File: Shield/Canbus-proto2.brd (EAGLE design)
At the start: 92.7 x 53.3 mm, 82 parts, among them J1 Digital_0_7, J2 Analog, J3 Digital_8_13, J4 Analog, J5 Digital_14_21

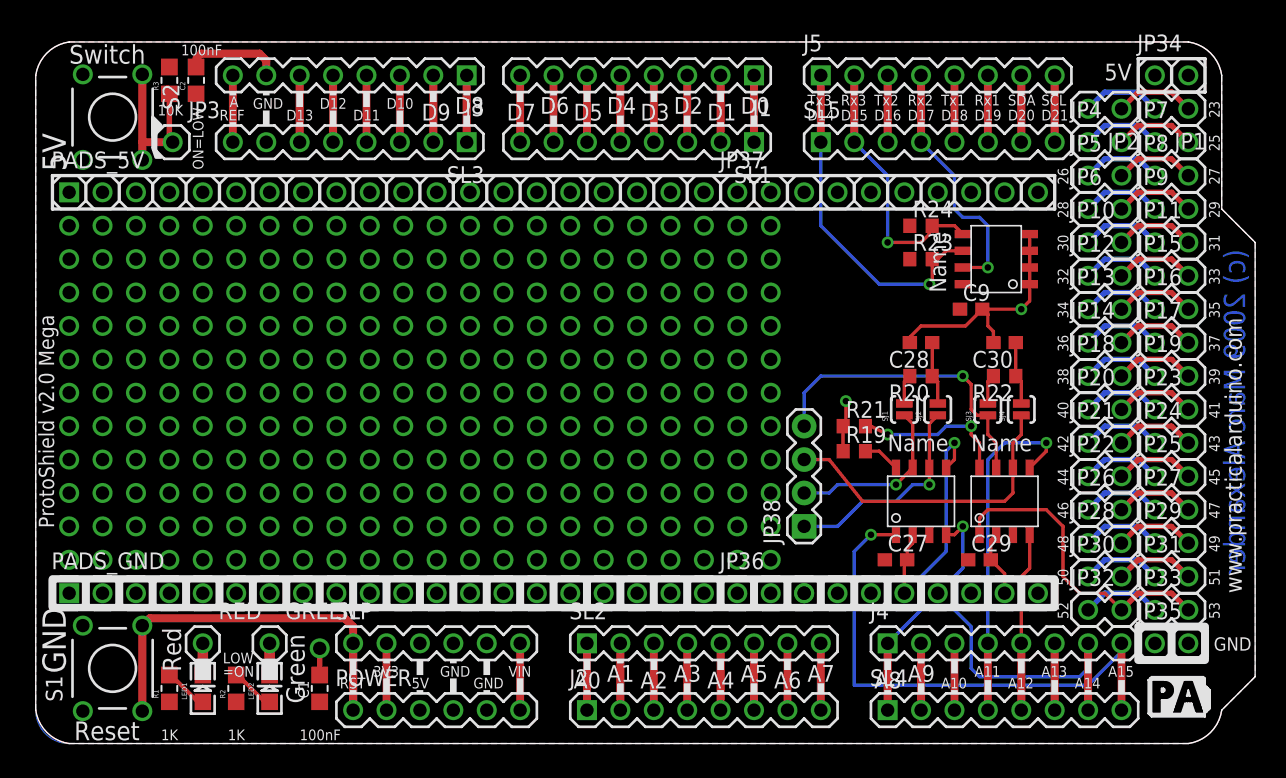
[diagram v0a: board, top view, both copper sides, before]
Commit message: Updated board design for canbus shield. There are now RJ45 ports for canbus outputs and a little SMD proto space.
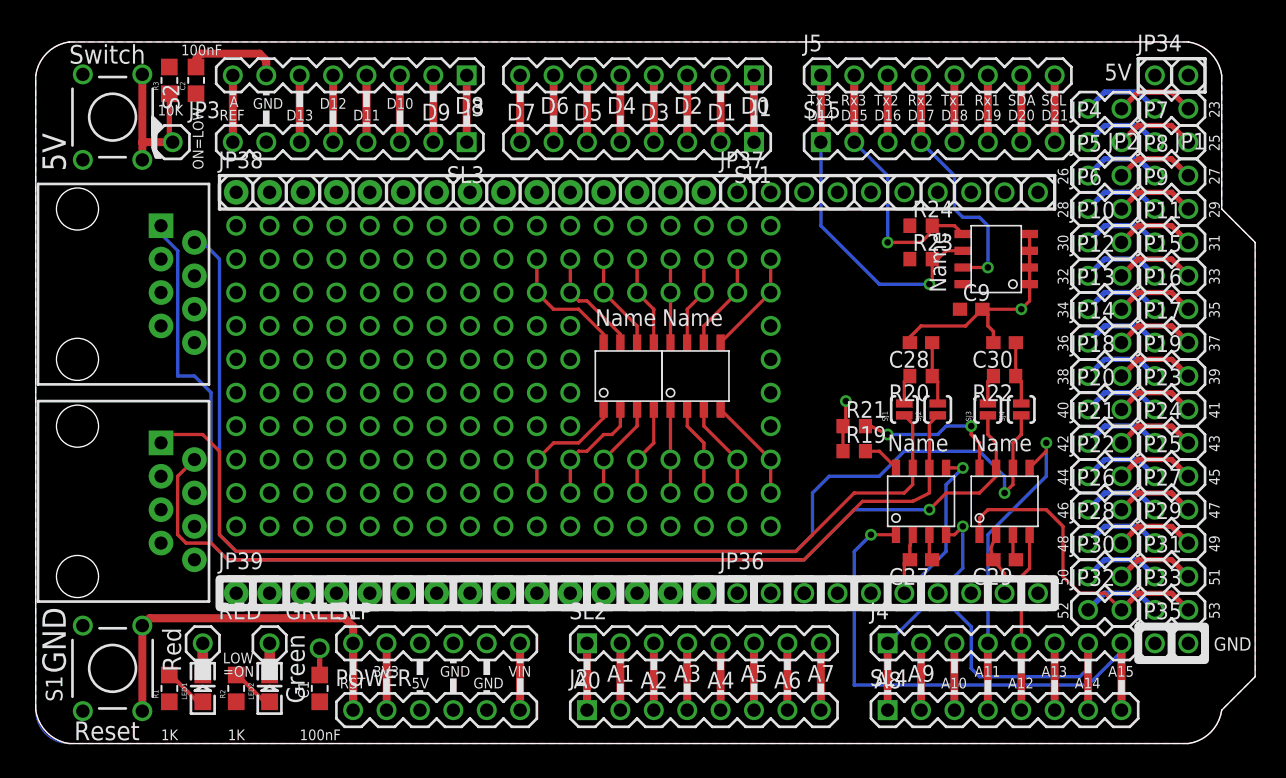
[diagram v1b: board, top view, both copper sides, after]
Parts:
- removed PADS_5V, PADS_GND: M20, SparkFun:1X20
- added JP39: M15, SparkFun-Connectors:1X15
- added U$1, U$2: RJ45-8PTH, SparkFun-Connectors:RJ45-8
- added U$3: SN65HVD234, ck_custom:SOIC8
- JP38: value (none) -> M15; device SparkFun-Connectors:1X04 -> SparkFun-Connectors:1X15
- U$4: value (none) -> SN65HVD234; device SparkFun:PRACTICALARDUINO-LOGO -> ck_custom:SOIC8
- moved JP38 50.1 mm to (15.2, 41.9), turned to 0 degrees
- moved U$4 48.4 mm to (42.5, 26.0)
- moved C27 1.91 mm to (67.3, 14.0), turned to 180 degrees
- moved C29 1.91 mm to (73.7, 14.0), turned to 180 degrees
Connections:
- new net B1: U$3.PIN8
- new net B10: U$4.PIN7
- new net B11: U$4.PIN6
- new net B12: U$4.PIN5
- new net B13: U$4.PIN4
- new net B14: U$4.PIN3
- new net B15: U$4.PIN2
- new net B16: U$4.PIN1
- new net B2: U$3.PIN7
- new net B3: U$3.PIN6
- new net B4: U$3.PIN5
- new net B5: U$3.PIN1
- new net B6: U$3.PIN2
- new net B7: U$3.PIN3
- new net B8: U$3.PIN4
- new net B9: U$4.PIN8
- net +3V3: now also JP38.1, JP38.10, JP38.11, JP38.12, JP38.13, JP38.14, JP38.15, JP38.2, JP38.3, JP38.4, JP38.5, JP38.6, JP38.7, JP38.8, JP38.9; no longer PADS_5V.1, PADS_5V.10, PADS_5V.11, PADS_5V.12, PADS_5V.13, PADS_5V.14, PADS_5V.15, PADS_5V.16, PADS_5V.17, PADS_5V.18, PADS_5V.19, PADS_5V.2, PADS_5V.20, PADS_5V.3, PADS_5V.4, PADS_5V.5, PADS_5V.6, PADS_5V.7, PADS_5V.8, PADS_5V.9
- net CANH0: now also U$2.1; no longer JP38.2
- net CANH1: now also U$1.1; no longer JP38.4
- net CANL0: now also U$2.2; no longer JP38.1
- net CANL1: now also U$1.2; no longer JP38.3
- net GND: now also JP39.1, JP39.10, JP39.11, JP39.12, JP39.13, JP39.14, JP39.15, JP39.2, JP39.3, JP39.4, JP39.5, JP39.6, JP39.7, JP39.8, JP39.9, U$1.3, U$1.7, U$2.3, U$2.7; no longer PADS_GND.1, PADS_GND.10, PADS_GND.11, PADS_GND.12, PADS_GND.13, PADS_GND.14, PADS_GND.15, PADS_GND.16, PADS_GND.17, PADS_GND.18, PADS_GND.19, PADS_GND.2, PADS_GND.20, PADS_GND.3, PADS_GND.4, PADS_GND.5, PADS_GND.6, PADS_GND.7, PADS_GND.8, PADS_GND.9
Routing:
- net CANL1: track 23.8 -> 97.1 mm, vias 0 -> 1
- net CANH1: track 23.6 -> 94.2 mm
- net CANH0: track 13.3 -> 72.4 mm, vias 1 -> 0
- net CANL0: track 16.4 -> 72.3 mm, vias 1 -> 0
- net B9: track 0.00 -> 9.57 mm, vias 0 -> 2
- net B16: track 0.00 -> 9.57 mm, vias 0 -> 2
- net B15: track 0.00 -> 8.67 mm, vias 0 -> 2
- net B10: track 0.00 -> 8.30 mm, vias 0 -> 2
- net B8: track 0.00 -> 7.93 mm, vias 0 -> 2
- net B4: track 0.00 -> 7.93 mm, vias 0 -> 2
- net B7: track 0.00 -> 7.40 mm, vias 0 -> 2
- net B3: track 0.00 -> 7.40 mm, vias 0 -> 2
- net B14: track 0.00 -> 7.40 mm, vias 0 -> 2
- net B11: track 0.00 -> 7.40 mm, vias 0 -> 2
- net B12: track 0.00 -> 6.88 mm, vias 0 -> 2
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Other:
- board text removed: "(c) 2009 Marc Alexander"
- board text removed: "ProtoShield v2.0 Mega"
- board text removed: "www.practicalarduino.com"

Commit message: Updated the board to be more better and junk.
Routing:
- net GND: track 41.6 -> 48.0 mm, vias 4 -> 6
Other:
- board size 92.7 x 53.3 mm -> 92.8 x 53 mm
- board text added: "CAN1"
- board text added: "CAN2"
- board text added: "Due CAN Shield V 1.0"
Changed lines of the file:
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@@
 <layer number="20" name="Dimension" color="15" fill="1" visible="yes" active="yes"/>
 <layer number="21" name="tPlace" color="16" fill="1" visible="yes" active="yes"/>
-<layer number="22" name="bPlace" color="14" fill="1" visible="no" active="yes"/>
+<layer number="22" name="bPlace" color="14" fill="1" visible="yes" active="yes"/>
 <layer number="23" name="tOrigins" color="15" fill="1" visible="yes" active="yes"/>
 <layer number="24" name="bOrigins" color="15" fill="1" visible="no" active="yes"/>
@@
 <board>
 <plain>
-<wire x1="0" y1="2.54" x2="2.54" y2="0" width="0" layer="20" curve="73.740878"/>
-<wire x1="87.63" y1="0" x2="90.17" y2="2.54" width="0" layer="20" curve="73.740878"/>
-<wire x1="90.17" y1="2.54" x2="92.71" y2="5.08" width="0" layer="20"/>
-<wire x1="92.71" y1="5.08" x2="92.71" y2="38.1" width="0" layer="20"/>
-<wire x1="92.71" y1="38.1" x2="90.17" y2="40.64" width="0" layer="20"/>
+<wire x1="0" y1="2.54" x2="-0.635" y2="0.635" width="0" layer="20" curve="73.740878"/>
+<wire x1="84.455" y1="0.635" x2="90.17" y2="2.54" width="0" layer="20" curve="73.740878"/>
+<wire x1="90.17" y1="2.54" x2="92.075" y2="6.985" width="0" layer="20"/>
+<wire x1="92.075" y1="6.985" x2="92.075" y2="40.005" width="0" layer="20"/>
+<wire x1="92.075" y1="40.005" x2="90.17" y2="40.64" width="0" layer="20"/>
 <wire x1="90.17" y1="40.64" x2="90.17" y2="50.8" width="0" layer="20"/>
 <wire x1="90.17" y1="50.8" x2="87.63" y2="53.34" width="0" layer="20" curve="73.740878"/>
@@
 <wire x1="78.1304" y1="44.45" x2="78.7654" y2="45.085" width="0.2032" layer="22"/>
 <wire x1="78.7654" y1="45.085" x2="78.7654" y2="46.355" width="0.2032" layer="22"/>
-<wire x1="2.54" y1="0" x2="87.63" y2="0" width="0" layer="20"/>
+<wire x1="-0.635" y1="0.635" x2="84.455" y2="0.635" width="0" layer="20"/>
 <text x="11.049" y="5.461" size="1.397" layer="21" font="vector" ratio="15" rot="R90">Red</text>
 <text x="20.447" y="3.048" size="1.397" layer="21" font="vector" ratio="15" rot="R90">Green</text>
-<text x="2.921" y="0.254" size="1.4224" layer="21" font="vector" ratio="15">Reset</text>
+<text x="2.286" y="2.921" size="1.4224" layer="21" font="vector" ratio="15" rot="R90">Reset</text>
 <text x="2.54" y="51.689" size="1.4224" layer="21" font="vector" ratio="15">Switch</text>
-<text x="2.286" y="5.334" size="1.778" layer="21" font="vector" ratio="16" rot="R90">GND</text>
-<text x="2.286" y="43.5102" size="1.778" layer="21" font="vector" ratio="16" rot="R90">5V</text>
 <text x="23.114" y="4.191" size="0.8128" layer="21" font="vector" ratio="15">RST</text>
 <text x="25.654" y="5.08" size="0.8128" layer="21" font="vector" ratio="15">3V3</text>
@@
 <text x="14.732" y="48.387" size="0.8128" layer="21" font="vector" ratio="15">A</text>
 <text x="16.51" y="48.26" size="0.8128" layer="21" font="vector" ratio="15">GND</text>
-<text x="20.066" y="0.254" size="0.8128" layer="21" font="vector" ratio="15">100nF</text>
-<text x="14.605" y="0.254" size="0.8128" layer="21" font="vector" ratio="15">1K</text>
-<text x="9.525" y="0.254" size="0.8128" layer="21" font="vector" ratio="15">1K</text>
+<text x="18.796" y="1.524" size="0.8128" layer="21" font="vector" ratio="15">100nF</text>
+<text x="14.605" y="1.524" size="0.8128" layer="21" font="vector" ratio="15">1K</text>
+<text x="9.525" y="1.524" size="0.8128" layer="21" font="vector" ratio="15">1K</text>
 <text x="9.271" y="47.752" size="0.8128" layer="21" font="vector" ratio="15">10K</text>
 <text x="11.049" y="52.324" size="0.8128" layer="21" font="vector" ratio="15">100nF</text>
@@
 <text x="78.5114" y="9.4742" size="0.8128" layer="21" font="vector" ratio="15" rot="R90">52</text>
 <text x="12.7508" y="43.6372" size="0.8128" layer="21" font="vector" ratio="15" rot="R90">ON=LOW</text>
-<text x="2.286" y="10.16" size="1.778" layer="22" font="vector" ratio="16" rot="MR270">GND</text>
-<text x="2.286" y="46.8122" size="1.778" layer="22" font="vector" ratio="16" rot="MR270">5V</text>
 <text x="60.579" y="47.371" size="0.8128" layer="22" font="vector" ratio="15" rot="MR0">D14</text>
 <text x="60.579" y="48.514" size="0.8128" layer="22" font="vector" ratio="15" rot="MR0">Tx3</text>
@@
 <vertex x="8.89" y="46.355"/>
 </polygon>
+<text x="91.44" y="10.795" size="1.4224" layer="21" rot="R90">Due CAN Shield V 1.0</text>
+<text x="90.17" y="10.795" size="1.4224" layer="22" rot="SMR90">Due CAN Shield V 1.0</text>
+<text x="6.35" y="38.1" size="1.778" layer="22" rot="SMR270">CAN2</text>
+<text x="6.35" y="21.59" size="1.778" layer="22" rot="SMR270">CAN1</text>
 </plain>
 <attributes>
@@
 <contactref element="U$2" pad="3"/>
 <contactref element="U$1" pad="3"/>
-<wire x1="71.12" y1="11.43" x2="68.58" y2="11.43" width="0" layer="19" extent="1-1"/>
+<via x="64.77" y="30.48" extent="1-16" drill="0.5"/>
+<via x="71.12" y="30.48" extent="1-16" drill="0.5"/>
+<wire x1="64.77" y1="30.48" x2="66.675" y2="30.48" width="0.254" layer="1"/>
+<wire x1="71.12" y1="30.48" x2="73.025" y2="30.48" width="0.254" layer="1"/>
+<wire x1="68.58" y1="11.43" x2="71.12" y2="11.43" width="0.4064" layer="1"/>
 </signal>
 <signal name="VIN">
@@
 <contactref element="JP38" pad="14"/>
 <contactref element="JP38" pad="15"/>
+<wire x1="15.24" y1="41.91" x2="15.24" y2="3.175" width="0" layer="19" extent="1-1"/>
 </signal>
 <signal name="CAN0-EN">

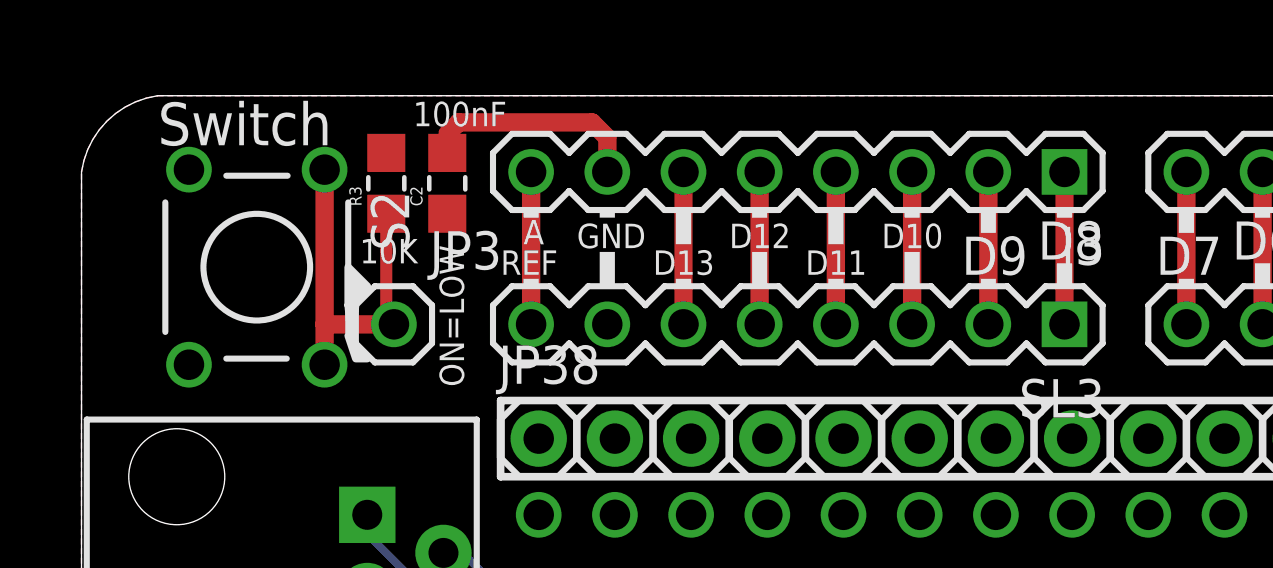
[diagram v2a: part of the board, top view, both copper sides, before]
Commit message: Removed momentary switch, added SCL1/SDA1
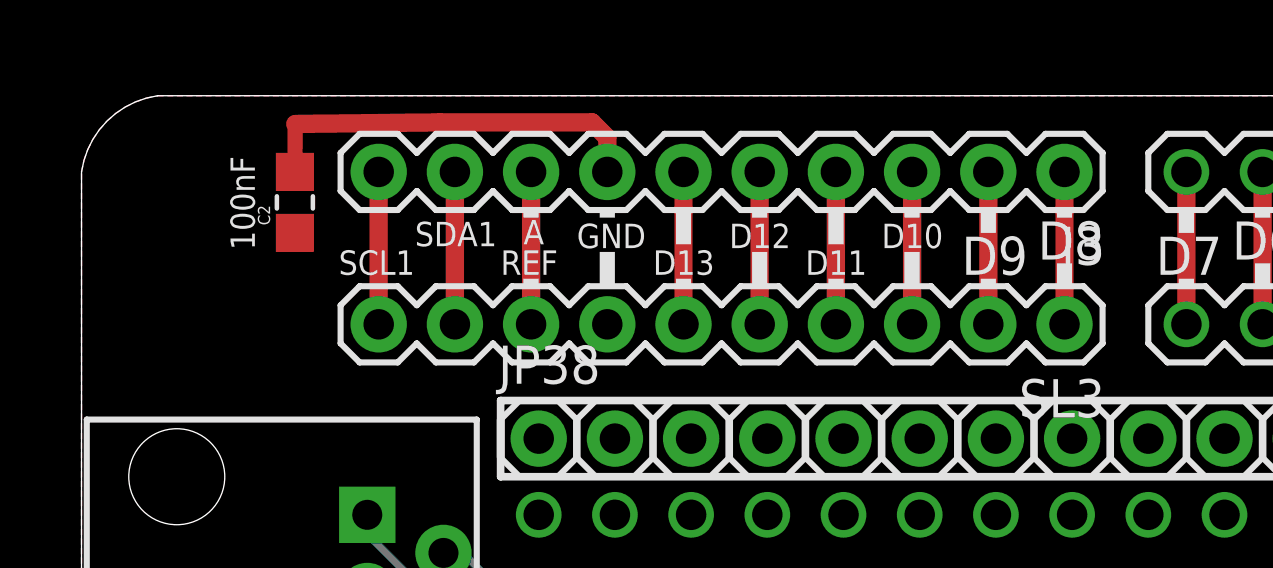
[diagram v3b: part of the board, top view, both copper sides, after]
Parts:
- removed JP3: SWITCH, SparkFun:1X01
- removed R3: 10K 0805, SparkFun:0805-LARGE
- removed S2: SWITCH, SparkFun:TACTILE-PTH
- J3, SL3: device SparkFun:1X08 -> SparkFun-Connectors:1X10
- moved C2 5.12 mm to (7.11, 49.8)
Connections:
- removed net N$6: JP3.1, R3.1, S2.1, S2.2
- new net SCL1: J3.10, SL3.10
- new net SDA1: J3.9, SL3.9
- net +3V3: no longer R3.2
- net GND: no longer S2.3, S2.4
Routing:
- net N$6: track 12.5 -> 0.00 mm
- net GND: track 48.0 -> 53.8 mm
- net SDA1: track 0.00 -> 5.08 mm
- net SCL1: track 0.00 -> 5.08 mm
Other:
- board text added: "SCL1"
- board text added: "SDA1"
- board text removed: "10K"
- board text removed: "ON="
- board text removed: "ON=LOW"
- board text removed: "Switch"
